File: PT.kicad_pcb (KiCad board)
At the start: 4 copper layers, 67 x 68 mm, 110 parts, among them J1 Conn_02x05_Odd_Even, J10 Screw_Terminal_01x05, J11 RJ45_Hanrun_HR911105A_Horizon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, J2 Conn_02x01, J3 Conn_02x01, J4 Conn_02x01, J5 Conn_02x01, J6 Screw_Terminal_01x02, J7 USB_C_Receptacle_USB2.0_16P, J8 Conn_02x01, J9 Conn_02x01, SW1 SW_MEC_5E, U1 STM32H563RITx, U10 LAN8742A, U2 INA241A1xD, U3 INA241A1xD, U4 INA241A1xD, U5 INA241A1xD, U6 ADS131A04, U7 AP2112K-3.3, U8 USBLC6-2SC6, U9 TJA1042T-3, Y1 25 MHz, Y2 16.384 MHz, Y3 25 MHz

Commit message: Initial release A1
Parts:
- F1, F2: footprint aprlprints:Fuse_0805_2012Metric-noct -> Fuse:Fuse_0805_2012Metric
- R4, R5, R6, R7: value 13.7R -> 13R; footprint Resistor_SMD:R_1210_3225Metric -> libpt:R_1206_3216Metric
- moved SW1 0.63 mm to (151.0, 93.7)
- moved C42 0.45 mm to (124.3, 121.8)
- moved R22 0.25 mm to (123.5, 128.3)
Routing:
- net ETH_TX_EN: track 12.2 -> 13.1 mm
- net ETH_TXD0: track 24.6 -> 25.3 mm
- net GND: vias 324 -> 323
- net +3.3V: vias 43 -> 42

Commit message: Pranked by propfeed and engine again
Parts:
- removed the C12 at (149.4, 84.1)
- removed the C13 at (136.3, 84.1)
- removed the C14 at (123.5, 84.2)
- removed the C15 at (110.5, 84.2)
- removed the C16 at (136.3, 89.1)
- removed the C17 at (132.6, 89.0)
- removed the C18 at (129.1, 89.0)
- removed the R10 at (129.1, 87.5)
- removed the R5 at (131.8, 79.3)
- removed the R6 at (118.8, 79.3)
- removed the R7 at (105.8, 79.3)
- removed the R8 at (136.3, 87.7)
- removed the U2 at (144.8, 84.1)
- removed the U4 at (118.8, 84.1)
- removed the U5 at (105.8, 84.1)
- removed U7: AP2112K-3.3, Package_TO_SOT_SMD:SOT-23-5
- added C25: 10nF, aprlprints:C_0603-noct, F.Cu at (133.5, 85.5)
- added C28: 10nF, aprlprints:C_0603-noct, F.Cu at (128.7, 85.6)
- added C31: 10nF, aprlprints:C_0603-noct, F.Cu at (126.0, 88.7)
- added NT1: NetTie_2, NetTie:NetTie-2_SMD_Pad0.5mm, F.Cu at (151.2, 82.6)
- added NT2: NetTie_2, NetTie:NetTie-2_SMD_Pad0.5mm, F.Cu at (126.0, 82.6)
- added NT3: NetTie_2, NetTie:NetTie-2_SMD_Pad0.5mm, F.Cu at (139.0, 82.6)
- added NT4: NetTie_2, NetTie:NetTie-2_SMD_Pad0.5mm, F.Cu at (113.3, 82.7)
- added R12: 100R, APRLPrints:R_0603, F.Cu at (135.8, 84.7)
- added R13: 100R, APRLPrints:R_0805, F.Cu at (137.6, 82.7)
- added R14: 100R, APRLPrints:R_0603, F.Cu at (135.8, 86.3)
- added R15: 100R, APRLPrints:R_0603, F.Cu at (126.4, 86.4)
- added R16: 100R, APRLPrints:R_0805, F.Cu at (124.5, 82.7)
- added R17: 100R, APRLPrints:R_0603, F.Cu at (126.4, 84.8)
- added R18: 100R, APRLPrints:R_0603, F.Cu at (123.7, 89.5)
- added R19: 100R, APRLPrints:R_0805, F.Cu at (111.8, 82.7)
- added R20: 100R, APRLPrints:R_0603, F.Cu at (123.7, 87.9)
- C19: value 6.8nF -> 10nF
- C29: renamed from C25; value 10pF -> 30pF
- C30: renamed from C27; value 10pF -> 30pF
- R10: renamed from R4; value 13R -> 100R; footprint libpt:R_1206_3216Metric -> APRLPrints:R_0805
- R11, R9: value 330R -> 100R; footprint aprlprints:R_0603-noct -> APRLPrints:R_0603
- U3: value INA241A1xD -> TPS7A2045PDBV; footprint Package_SO:SOIC-8_3.9x4.9mm_P1.27mm -> Package_TO_SOT_SMD:SOT-23-5
- moved U3 36.4 mm to (150.8, 115.2), turned to 180 degrees
- moved R11 14.8 mm to (140.1, 89.3), turned to 180 degrees
- moved C19 12.4 mm to (137.8, 88.5), turned to -90 degrees
- moved R9 7.48 mm to (140.1, 87.7)
- moved R10 5.98 mm to (149.8, 82.7), turned to 0 degrees
- renumbered C2 to C1, C3 to C10, C7 to C11, C9 to C12, C29 to C13, C30 to C14, C31 to C15, C32 to C16, C33 to C17, C34 to C18, C4 to C2, C23 to C20, C24 to C21, C26 to C22, C28 to C23, C20 to C24, C21 to C26, C22 to C27, C5 to C3, C38 to C32, C40 to C33, C42 to C34, C43 to C35, C37 to C36, C44 to C37, C45 to C38, C36 to C39, C6 to C4, C46 to C40, C39 to C41, C41 to C42, C8 to C5, C10 to C6, C11 to C7, C35 to C8, C1 to C9, F2 to F1, F1 to F2, J7 to J2, J2 to J3, J3 to J4, J4 to J5, J5 to J6, J6 to J7, R15 to R1, R16 to R2, R17 to R21, R18 to R22, R20 to R23, R21 to R24, R23 to R25, R24 to R26, R22 to R27, R19 to R28, R26 to R29, R1 to R3, R25 to R30, R2 to R4, R3 to R5, R12 to R6, R13 to R7, R14 to R8, U8 to U1, U1 to U2, U6 to U4, U9 to U5, U10 to U6
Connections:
- C19 pad 1: /Analog/AIN4+ -> /Analog/AIN1+
- C19 pad 2: GND -> /Analog/AIN1-
- J3 pad 2: Net-(J2-Pin_2) -> /Analog/AIN1_SENSE+
- J4 pad 2: Net-(J3-Pin_2) -> /Analog/AIN2_SENSE+
- J5 pad 2: Net-(J4-Pin_2) -> /Analog/AIN3_SENSE+
- J6 pad 2: Net-(J5-Pin_2) -> /Analog/AIN4_SENSE+
- R10 pad 1: Net-(J2-Pin_2) -> /Analog/AIN1_SENSE+
- R10 pad 2: GND -> /Analog/AIN1_SENSE-
- R11 pad 1: Net-(R11-Pad1) -> /Analog/AIN1_SENSE-
- R11 pad 2: /Analog/AIN4+ -> /Analog/AIN1-
- R9 pad 1: Net-(R9-Pad1) -> /Analog/AIN1_SENSE+
- R9 pad 2: /Analog/AIN2+ -> /Analog/AIN1+
- U3 pad 1: GND -> +5V
- U3 pad 3: GND -> +5V
- U3 pad 4: GND -> unconnected-(U3-NC-Pad4)
- U3 pad 5: Net-(R9-Pad1) -> +3.3V
- U4 pad 1: GND -> /Analog/AIN1-
- U4 pad 3: GND -> /Analog/AIN2-
- U4 pad 5: GND -> /Analog/AIN3-
- U4 pad 7: GND -> /Analog/AIN4-
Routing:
- net Net-(R11-Pad1): track 17.1 -> 0.00 mm
- net /Analog/AIN4_SENSE+: track 0.00 -> 14.9 mm
- net /Analog/AIN4_SENSE-: track 0.00 -> 13.6 mm
- net /Analog/AIN1_SENSE-: track 0.00 -> 12.7 mm
- net /Analog/AIN1_SENSE+: track 0.00 -> 11.3 mm
- net Net-(R8-Pad1): track 11.0 -> 0.00 mm
- net /Analog/AIN3-: track 0.00 -> 9.13 mm
- net /Analog/AIN4-: track 0.00 -> 8.27 mm
- net /Analog/AIN1-: track 0.00 -> 7.83 mm
- net Net-(R10-Pad1): track 7.79 -> 0.00 mm
- net /Analog/AIN2-: track 0.00 -> 7.59 mm
- net /Analog/AIN2+: track 3.68 -> 8.73 mm
- net /Analog/AIN3_SENSE+: track 0.00 -> 4.60 mm
- net /Analog/AIN2_SENSE-: track 0.00 -> 4.47 mm
- net /Analog/AIN3+: track 4.19 -> 7.99 mm
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- added copper zone on F.Cu, net /Analog/AIN1_SENSE+
- added copper zone on F.Cu, net /Analog/AIN2_SENSE+
- added copper zone on F.Cu, net /Analog/AIN3_SENSE+
- added copper zone on F.Cu, net /Analog/AIN4_SENSE+
- removed copper zone on F.Cu, net Net-(J2-Pin_2)
- removed copper zone on F.Cu, net Net-(J3-Pin_2)
- removed copper zone on F.Cu, net Net-(J4-Pin_2)
- removed copper zone on F.Cu, net Net-(J5-Pin_2)

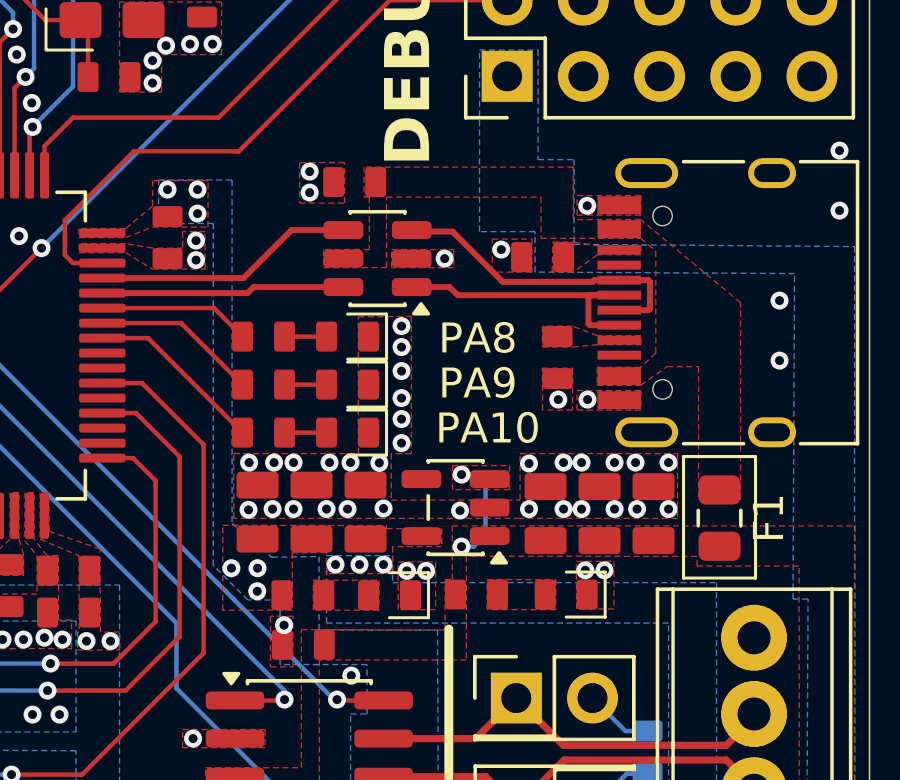
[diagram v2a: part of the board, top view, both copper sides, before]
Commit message: Swap TPS7A20 for LP5907 (Daniel yelled at me again)
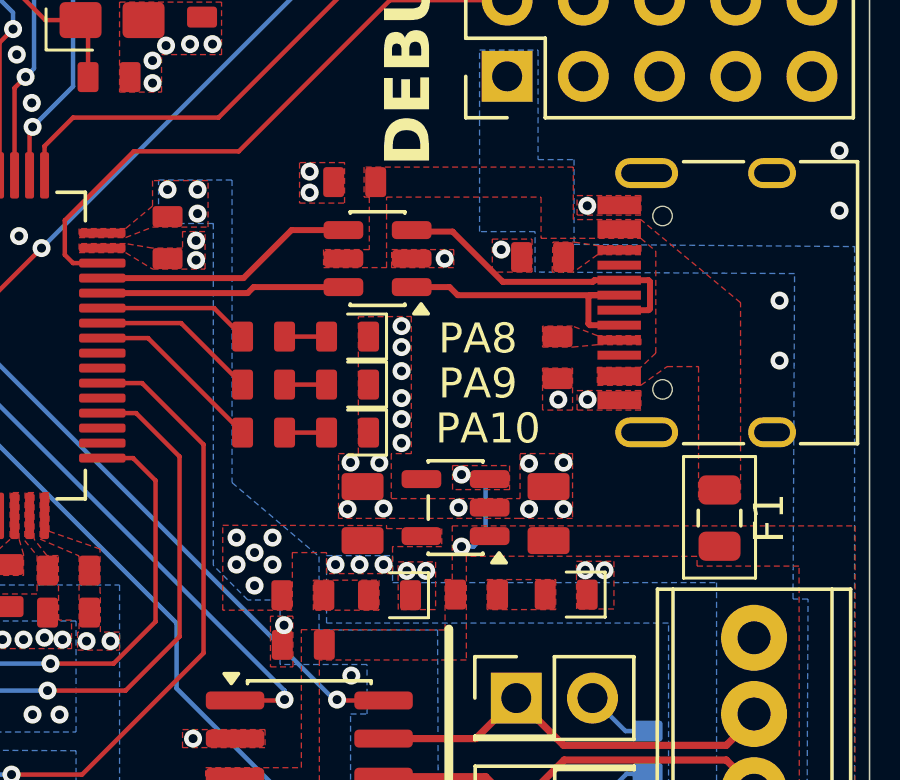
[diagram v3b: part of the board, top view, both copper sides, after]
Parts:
- removed the C14 at (155.6, 115.4)
- removed the C15 at (157.4, 115.4)
- removed the C17 at (146.0, 115.4)
- removed the C18 at (147.8, 115.4)
- U3: value TPS7A2045PDBV -> LP5907MFX-3.3
- moved C14 3.50 mm to (147.7, 115.4)
- moved C13 0.10 mm to (153.9, 115.4)
- renumbered C16 to C14, C19 to C15, C20 to C16, C21 to C17, C22 to C18, C23 to C19, C24 to C20, C25 to C21, C26 to C22, C27 to C23, C28 to C24, C29 to C25, C30 to C26, C31 to C27, C32 to C28, C33 to C29, C34 to C30, C35 to C31, C36 to C32, C37 to C33, C38 to C34, C39 to C35, C40 to C36, C41 to C37, C42 to C38, NT3 to NT2, NT2 to NT3
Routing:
- net GND: vias 303 -> 287
- net +3.3V: vias 38 -> 41
